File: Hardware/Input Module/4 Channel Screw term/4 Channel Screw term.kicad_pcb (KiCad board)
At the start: 2 copper layers, 43.4 x 31.5 mm, 22 parts, among them J1 Screw_Terminal_01x06, J2 Screw_Terminal_01x06, J5 Conn_01x12_Male, U1 LTV-847S, U2 74HC7014

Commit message: Gerber Upload Ordered version
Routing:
- net Net-(R2-Pad1): track 20.3 -> 19.1 mm
- net Net-(R4-Pad1): track 16.0 -> 15.0 mm

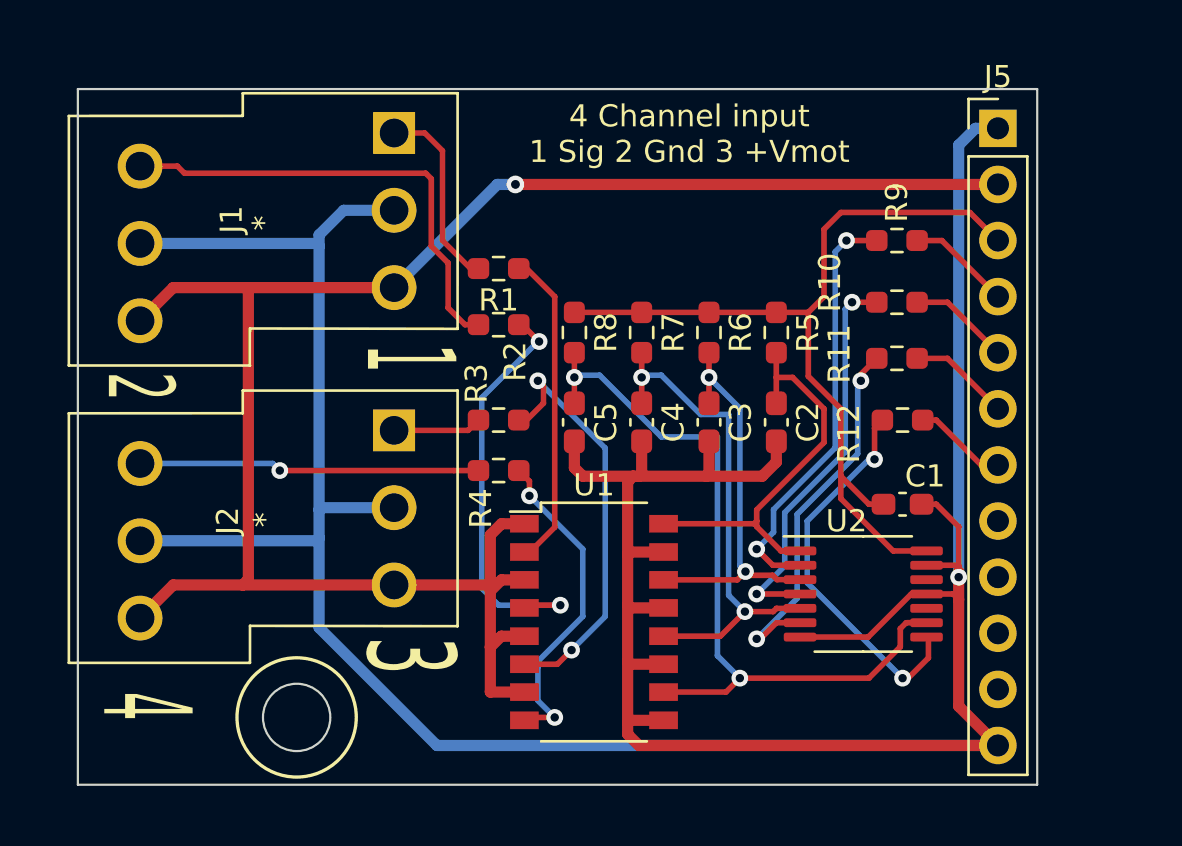
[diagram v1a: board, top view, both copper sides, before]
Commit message: redesigned input and output modules, cleaned some files, ordered 10 of each
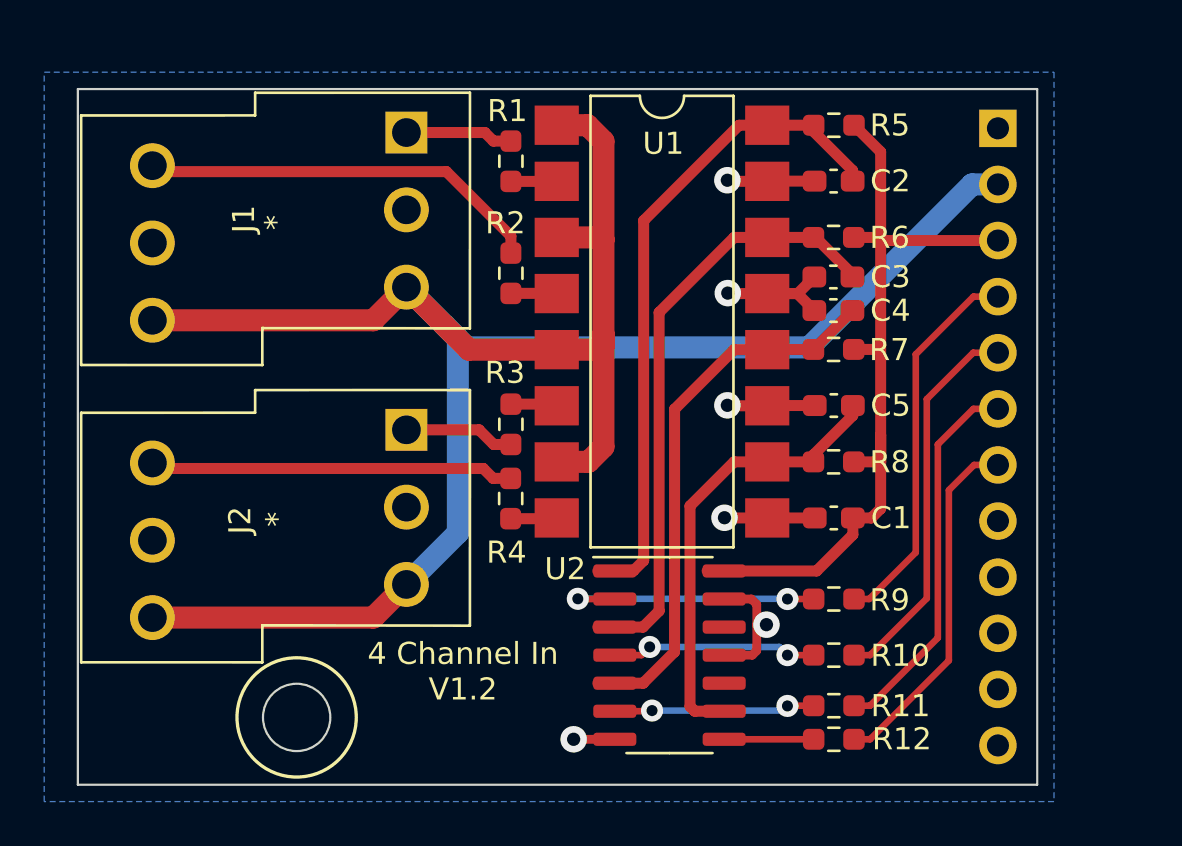
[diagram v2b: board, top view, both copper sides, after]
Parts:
- J5: moved to B.Cu
- U1: footprint Package_SO:SOP-16_4.4x10.4mm_P1.27mm -> Package_DIP:SMDIP-16_W9.53mm
- U2: footprint Package_SO:TSSOP-14_4.4x5mm_P0.65mm -> Package_SO:SO-14_3.9x8.65mm_P1.27mm
- moved R9 16.5 mm to (178.0, 84.8)
- moved R10 16.2 mm to (178.0, 87.3)
- moved R11 16.0 mm to (178.0, 89.6)
- moved R12 14.8 mm to (178.0, 91.2)
- moved U1 13.9 mm to (170.2, 72.2)
- moved R8 13.1 mm to (178.0, 78.6), turned to 180 degrees
- moved C5 11.8 mm to (178.0, 76.0), turned to 180 degrees
- moved C2 11.2 mm to (178.0, 65.9), turned to 180 degrees
- moved C4 10.0 mm to (178.0, 71.8), turned to 180 degrees
- moved R5 9.74 mm to (178.0, 63.4), turned to 180 degrees
- moved U2 9.20 mm to (170.6, 87.3)
- moved R7 8.72 mm to (178.0, 73.5), turned to 180 degrees
- moved C3 8.66 mm to (178.0, 70.2), turned to 180 degrees
- moved R6 7.10 mm to (178.0, 68.4), turned to 180 degrees
- moved R1 4.89 mm to (163.4, 65.0), turned to 90 degrees
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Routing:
- net GND: track 168.7 -> 26.3 mm, vias 1 -> 6
- net Net-(R2-Pad1): track 19.1 -> 2.08 mm, vias 2 -> 0
- net Net-(R3-Pad1): track 19.0 -> 2.11 mm, vias 2 -> 0
- net Net-(C5-Pad1): track 35.1 -> 19.6 mm, vias 2 -> 0
- net +15V: track 85.4 -> 99.7 mm, vias 1 -> 0
- net Net-(R12-Pad2): track 17.5 -> 4.05 mm, vias 2 -> 0
- net Net-(J5-Pad5): track 4.61 -> 17.5 mm
- net Net-(R4-Pad1): track 15.0 -> 2.10 mm, vias 2 -> 0
- net Net-(J5-Pad4): track 4.71 -> 17.4 mm
- net Net-(J5-Pad6): track 4.61 -> 17.2 mm
- net Net-(R1-Pad1): track 14.4 -> 2.08 mm
- net Net-(C2-Pad1): track 18.2 -> 30.4 mm
- net Net-(J5-Pad7): track 4.25 -> 16.2 mm
- net Net-(C3-Pad1): track 18.2 -> 27.6 mm, vias 2 -> 0
- net Net-(R10-Pad2): track 18.0 -> 9.31 mm
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- added copper zone on B.Cu, net GND
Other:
- board text added: "4 Channel In V1.2"
- board text removed: "1"
- board text removed: "2"
- board text removed: "3"
- board text removed: "4"
- board text removed: "4 Channel input 1 Sig 2 Gnd 3 +Vmot"

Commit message: Random changes
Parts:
- moved J1 46.1 mm to (186.9, 88.5), turned to 90 degrees
- moved J5 45.5 mm to (148.6, 90.2), turned to 0 degrees
- moved J2 39.9 mm to (186.9, 75.0), turned to 90 degrees
- moved R12 36.1 mm to (156.0, 62.5), turned to 0 degrees
- moved R5 34.8 mm to (156.0, 90.3), turned to 0 degrees
- moved R11 33.7 mm to (156.0, 64.0), turned to 0 degrees
- moved C2 31.0 mm to (156.0, 87.8), turned to 0 degrees
- moved R10 30.4 mm to (156.0, 66.3), turned to 0 degrees
- moved R6 27.6 mm to (156.0, 85.2), turned to 0 degrees
- moved R9 27.1 mm to (156.0, 68.9), turned to 0 degrees
- moved C3 25.6 mm to (156.0, 83.4), turned to 0 degrees
- moved R1 24.8 mm to (170.6, 88.7), turned to -90 degrees
- moved C4 24.2 mm to (156.0, 81.9), turned to 0 degrees
- moved C1 23.6 mm to (156.0, 72.5), turned to 0 degrees
- moved R7 22.9 mm to (156.0, 80.2), turned to 0 degrees
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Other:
- outline, holes or cut-outs redrawn
